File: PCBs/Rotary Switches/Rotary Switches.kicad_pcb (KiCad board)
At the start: 2 copper layers, 37.1 x 33.7 mm, 8 parts, among them J1 Conn_01x03_Pin, SW1 A12505RNCQ

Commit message: Release Rotary Switch PCB version 1.2 with ON/OFF solder jumper
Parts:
- added JP1: ON/OFF, Jumper:SolderJumper-2_P1.3mm_Open_Pad1.0x1.5mm, B.Cu at (123.0, 68.8)
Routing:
- net /GND: track 6.87 -> 22.1 mm
- net /TAP_1: track 14.5 -> 28.6 mm
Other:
- board text added: "ARC-210 v1.2 Rotary Switch"
- board text added: "Solder Here for On/Off"
- board text removed: "ARC-210 v1.1 Rotary Switch"

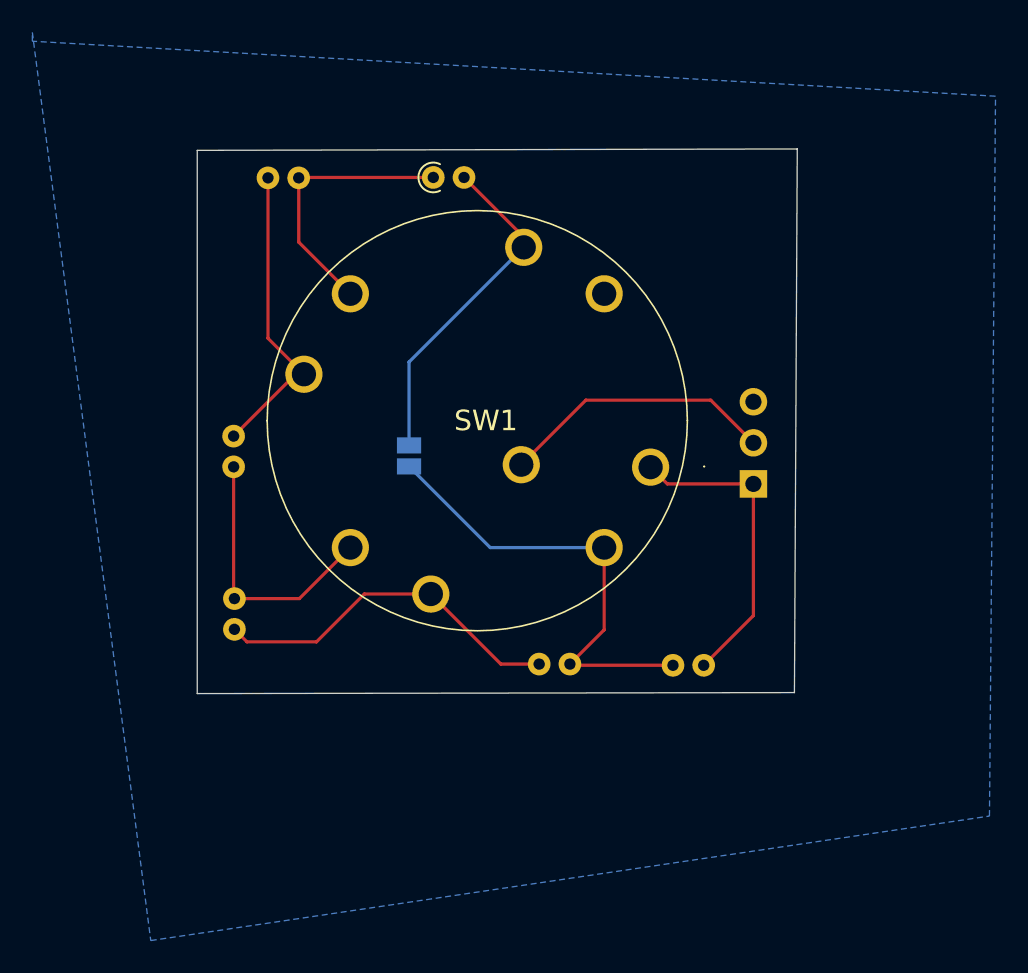
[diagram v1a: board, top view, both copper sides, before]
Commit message: Publish rotary switch PCB version 2.0
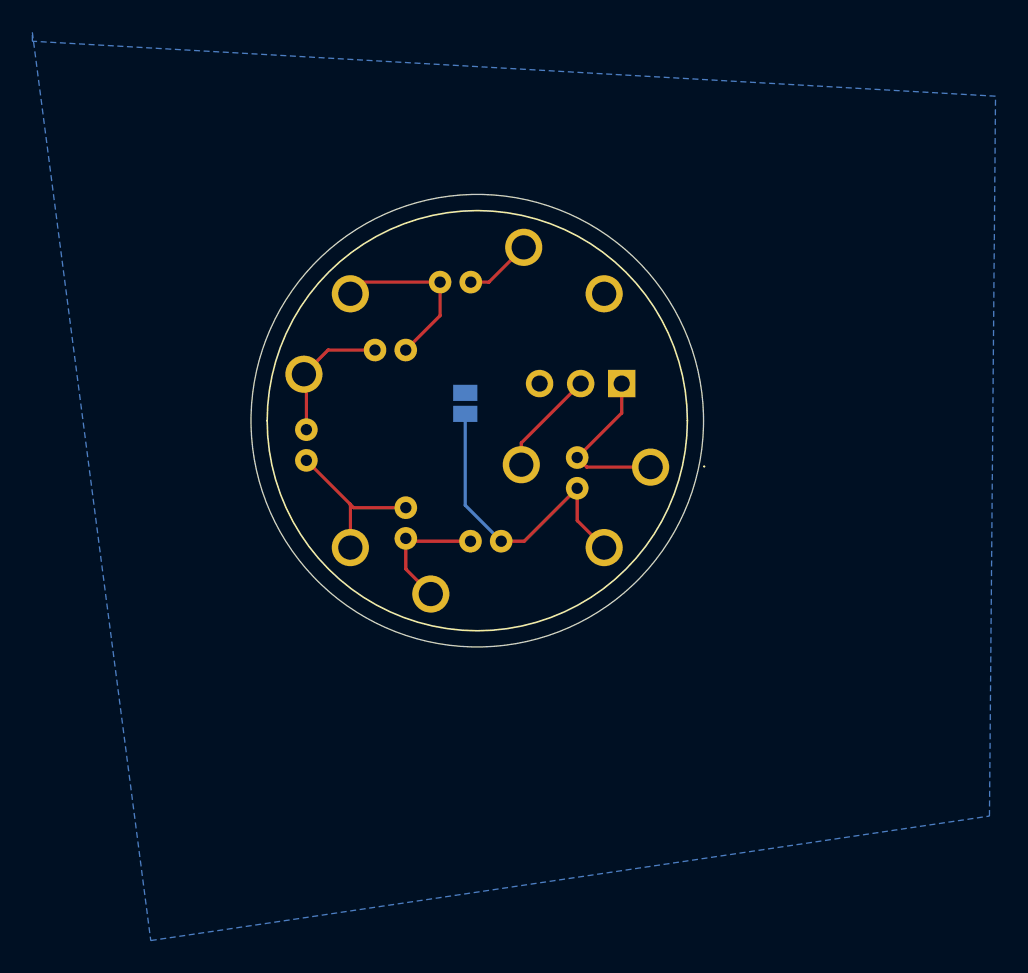
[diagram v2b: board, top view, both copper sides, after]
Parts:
- R6: moved to B.Cu
- moved R1 15.0 mm to (133.4, 68.8), turned to -90 degrees
- moved R5 12.5 mm to (120.9, 62.2)
- moved R3 12.0 mm to (122.8, 73.8)
- moved J1 10.2 mm to (136.2, 64.3), turned to 90 degrees
- moved R2 8.71 mm to (128.8, 74.0)
- moved R6 6.49 mm to (125.0, 58.0)
- moved JP1 4.76 mm to (126.5, 65.5)
- moved R4 4.52 mm to (116.7, 69.0)
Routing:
- net /GND: track 22.1 -> 5.81 mm
- net /TAP_2: track 22.2 -> 8.16 mm
- net /ROTARY_ADC: track 17.1 -> 6.54 mm
- net /TAP_4: track 19.0 -> 9.03 mm
- net /TAP_1: track 28.6 -> 19.2 mm
- net /+3V3: track 19.3 -> 10.5 mm
- net /TAP_3: track 16.6 -> 10.0 mm
- net /TAP_5: track 18.4 -> 12.5 mm
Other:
- board size 37.1 x 33.7 mm -> 28 x 28 mm
- board text added: "ARC-210 v2.0"
- board text removed: "ARC-210 v1.2 Rotary Switch"
- board text removed: "https://github.com/dgdimick"
